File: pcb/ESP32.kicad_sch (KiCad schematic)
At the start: 27 parts, among them J5 SPKR, SW1 BOOT, SW2 RESET, U3 SN74LV1T34DBV, U5 MAX98357A, U8 ESP32-S3-WROOM-2-N32R16V

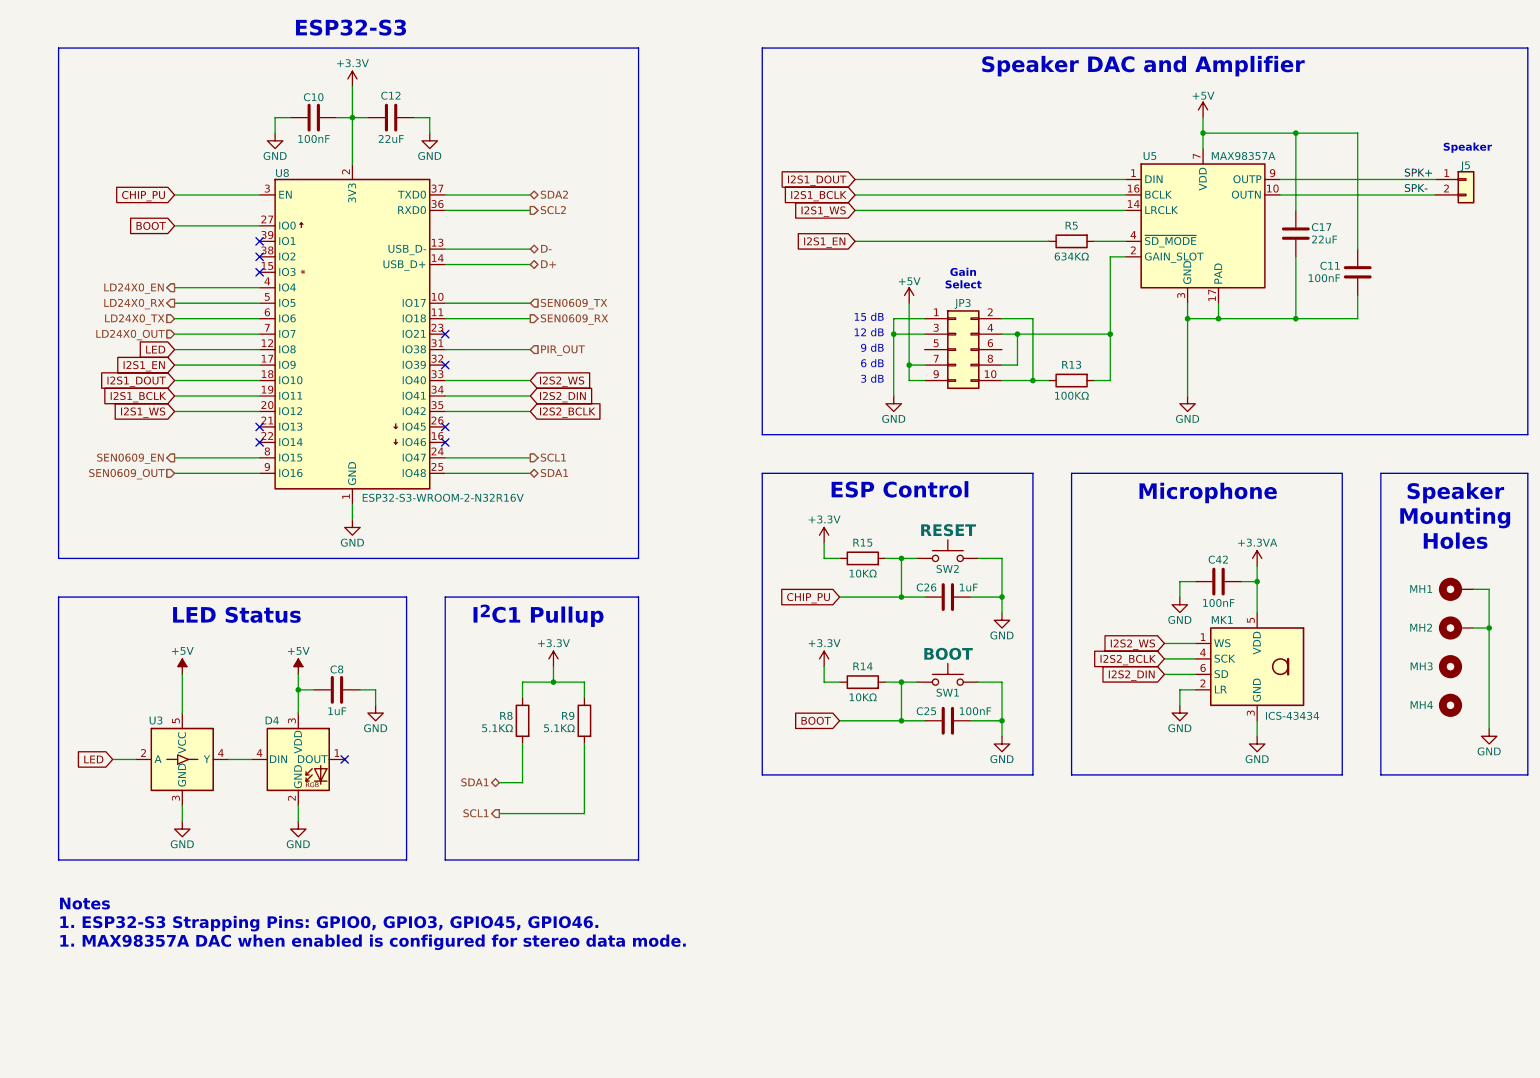
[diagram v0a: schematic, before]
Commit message: Rev A Updates
Support LD2410S and LD2420 Radars in same connector as C4001. Now using 3.3V instead of 5V.
Removed Power control for Radars.
Added DS18S20 to measure CO sensor temperature directly.
Reworked SHT4X layout to reduce thermal transfer.
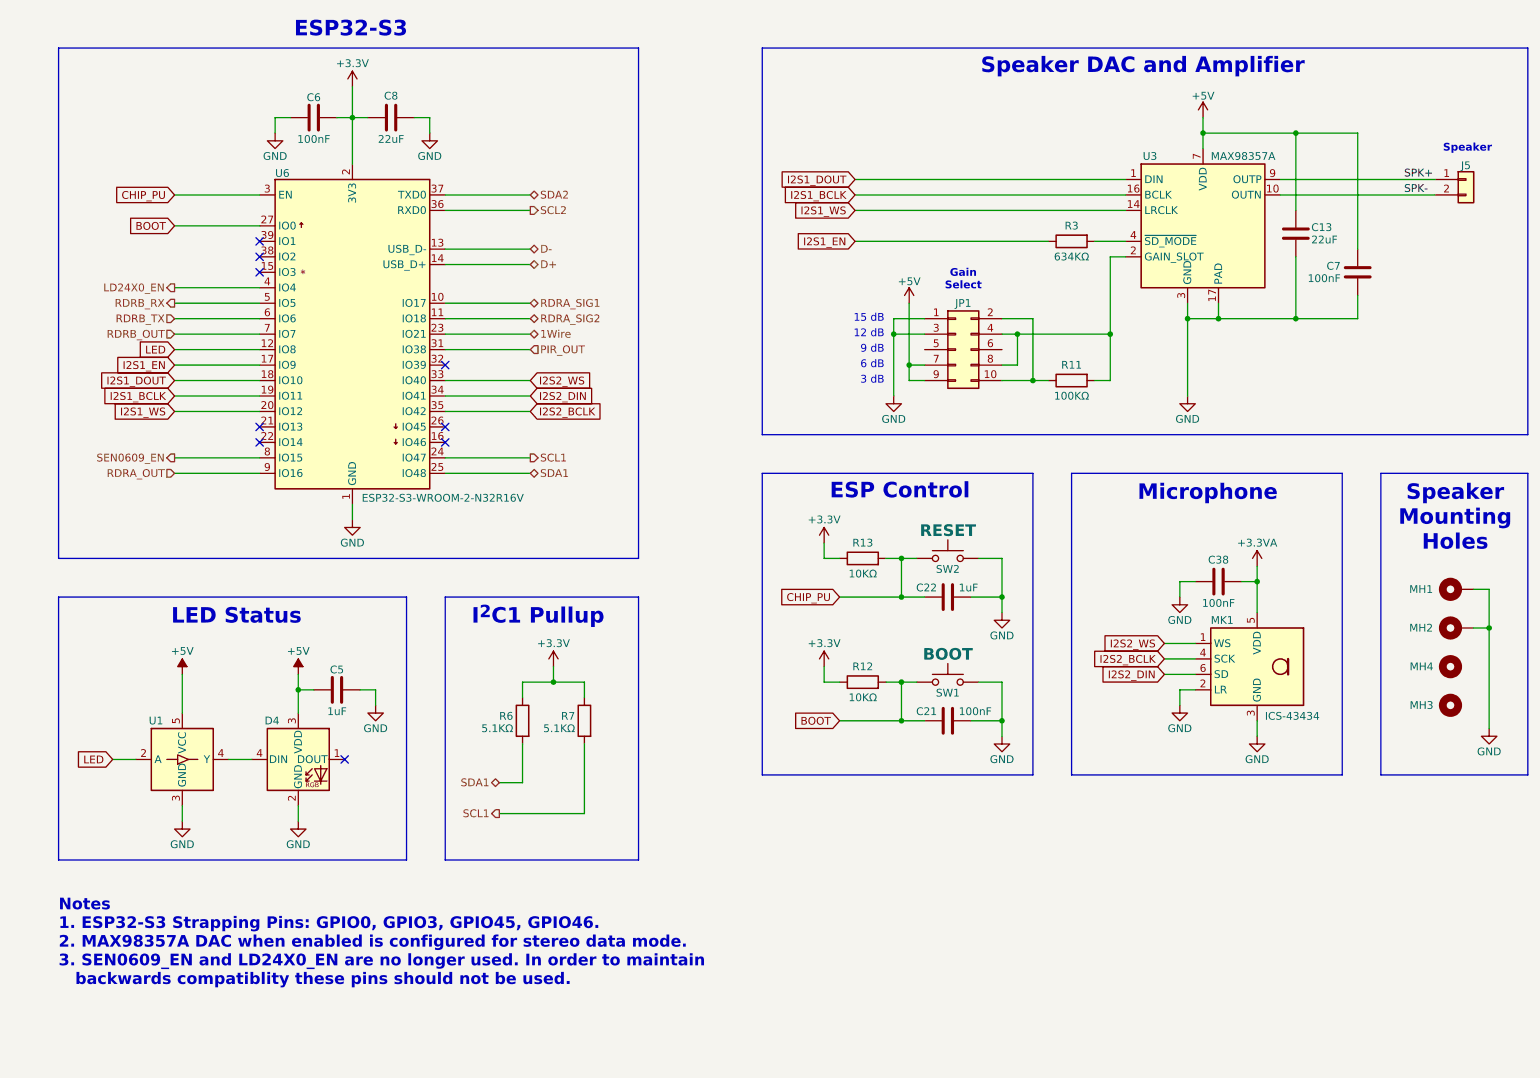
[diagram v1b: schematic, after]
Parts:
- renumbered C17 to C13, C25 to C21, C26 to C22, C42 to C38, C8 to C5, C10 to C6, C11 to C7, C12 to C8, JP3 to JP1, MH4 to MH3, MH3 to MH4, R13 to R11, R14 to R12, R15 to R13, R5 to R3, R8 to R6, R9 to R7, U3 to U1, U5 to U3, U8 to U6
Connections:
- net 1Wire: now reaches U6.23 (IO21)
- net LD24X0_OUT renamed RDRB_OUT
- net LD24X0_RX renamed RDRB_RX
- net LD24X0_TX renamed RDRB_TX
- net SEN0609_OUT renamed RDRA_OUT
- net SEN0609_RX renamed RDRA_SIG2
- net SEN0609_TX renamed RDRA_SIG1
- no-connect marks 10 -> 9
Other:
- note added: "Notes 1. ESP32-S3 Strapping Pins: GPIO0, GPIO3, GPIO45, GPIO46. 2. MAX98357A DAC when enabled is configured for stereo data mode. 3. SEN0609_EN and LD24X0_EN are no longer used. In order to maintain backwards compatiblity these pins should not be used."
- note removed: "Notes 1. ESP32-S3 Strapping Pins: GPIO0, GPIO3, GPIO45, GPIO46. 1. MAX98357A DAC when enabled is configured for stereo data mode."
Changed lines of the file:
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@@
 	(title_block
 		(title "ESPHome Parking Assistant")
-		(date "2025-04-18")
-		(rev "A")
+		(date "2025-09-23")
+		(rev "B")
 		(company "Mike Lawrence")
+		(comment 1 "Rev A: Fixed Rev - mistakes.")
+		(comment 2 "Rev B: Support for LD2410S/LD2420 and temp sensor for CO sensor.")
 	)
 	(rectangle
@@
 		)
 	)
-	(text "Notes\n1. ESP32-S3 Strapping Pins: GPIO0, GPIO3, GPIO45, GPIO46.\n1. MAX98357A DAC when enabled is configured for stereo data mode."
+	(text "Notes\n1. ESP32-S3 Strapping Pins: GPIO0, GPIO3, GPIO45, GPIO46.\n2. MAX98357A DAC when enabled is configured for stereo data mode.\n3. SEN0609_EN and LD24X0_EN are no longer used. In order to maintain\n   backwards compatiblity these pins should not be used."
 		(exclude_from_sim no)
 		(at 25.4 165.1 0)
@@
 	)
 	(no_connect
-		(at 88.9 72.39)
-	)
-	(no_connect
 		(at 58.42 59.69)
 	)
@@
 	(wire
 		(pts
+			(xy 88.9 72.39) (xy 102.87 72.39)
+		)
+		(stroke
+			(width 0)
+			(type default)
+		)
+	)
+	(wire
+		(pts
 			(xy 213.36 39.37) (xy 213.36 41.91)
 		)
@@
 		)
 	)
-	(hierarchical_label "LD24X0_TX"
+	(hierarchical_label "RDRB_TX"
 		(shape input)
 		(at 44.45 69.85 180)
@@
 		)
 	)
-	(hierarchical_label "LD24X0_RX"
+	(hierarchical_label "RDRA_SIG1"
+		(shape bidirectional)
+		(at 102.87 67.31 0)
+		(effects
+			(font
+				(size 1.27 1.27)
+			)
+			(justify left)
+		)
+	)
+	(hierarchical_label "RDRB_RX"
 		(shape output)
 		(at 44.45 67.31 180)
@@
 		)
 	)
-	(hierarchical_label "SEN0609_OUT"
-		(shape input)
-		(at 44.45 95.25 180)
+	(hierarchical_label "1Wire"
+		(shape bidirectional)
+		(at 102.87 72.39 0)
 		(effects
 			(font
 				(size 1.27 1.27)
 			)
-			(justify right)
+			(justify left)
 		)
 	)
-	(hierarchical_label "SEN0609_TX"
+	(hierarchical_label "RDRA_OUT"
 		(shape input)
-		(at 102.87 67.31 0)
+		(at 44.45 95.25 180)
 		(effects
 			(font
 				(size 1.27 1.27)
 			)
-			(justify left)
+			(justify right)
 		)
 	)
@@
 		)
 	)
-	(hierarchical_label "LD24X0_OUT"
+	(hierarchical_label "RDRB_OUT"
 		(shape input)
 		(at 44.45 72.39 180)
@@
 		)
 	)
-	(hierarchical_label "SDA2"
+	(hierarchical_label "RDRA_SIG2"
 		(shape bidirectional)
-		(at 102.87 49.53 0)
+		(at 102.87 69.85 0)
 		(effects
 			(font
@@
 		)
 	)
-	(hierarchical_label "SEN0609_RX"
-		(shape output)
-		(at 102.87 69.85 0)
+	(hierarchical_label "SDA2"
+		(shape bidirectional)
+		(at 102.87 49.53 0)
 		(effects
 			(font
@@
 		(on_board yes)
 		(dnp no)
-		(property "Reference" "MH3"
+		(property "Reference" "MH4"
 			(at 251.206 127 0)
 			(effects
@@
 			(project "ESPHome-Indoor-Multi-Sensor"
 				(path "/e74956a0-c576-42e7-be96-7ce5c3135988/bd75fc22-91af-4c71-b8b1-dfd5c5fbd52d"
-					(reference "MH3")
+					(reference "MH4")
 					(unit 1)
 				)
@@
 		(on_board yes)
 		(dnp no)
-		(property "Reference" "MH4"
+		(property "Reference" "MH3"
 			(at 251.206 133.35 0)
 			(effects
@@
 			(project "ESPHome-Indoor-Multi-Sensor"
 				(path "/e74956a0-c576-42e7-be96-7ce5c3135988/bd75fc22-91af-4c71-b8b1-dfd5c5fbd52d"
-					(reference "MH4")
+					(reference "MH3")
 					(unit 1)
 				)
@@
 		(on_board yes)
 		(dnp no)
-		(property "Reference" "U5"
+		(property "Reference" "U3"
 			(at 203.454 43.18 0)
 			(effects
@@
 			(project "ESPHome-Indoor-Multi-Sensor"
 				(path "/e74956a0-c576-42e7-be96-7ce5c3135988/bd75fc22-91af-4c71-b8b1-dfd5c5fbd52d"
-					(reference "U5")
+					(reference "U3")
 					(unit 1)
 				)
@@
 		(on_board yes)
 		(dnp no)
-		(property "Reference" "R14"
+		(property "Reference" "R12"
 			(at 157.48 127 90)
 			(effects
@@
 			(project "ESPHome-Indoor-Multi-Sensor"
 				(path "/e74956a0-c576-42e7-be96-7ce5c3135988/bd75fc22-91af-4c71-b8b1-dfd5c5fbd52d"
-					(reference "R14")
+					(reference "R12")
 					(unit 1)
 				)
@@
 		(on_board yes)
 		(dnp no)
-		(property "Reference" "C42"
+		(property "Reference" "C38"
 			(at 215.9 109.474 90)
 			(effects
@@
 			(project "ESPHome-Indoor-Multi-Sensor"
 				(path "/e74956a0-c576-42e7-be96-7ce5c3135988/bd75fc22-91af-4c71-b8b1-dfd5c5fbd52d"
-					(reference "C42")
+					(reference "C38")
 					(unit 1)
 				)
@@
 		(on_board yes)
 		(dnp no)
-		(property "Reference" "JP3"
+		(property "Reference" "JP1"
 			(at 173.99 67.31 0)
 			(effects
@@
 			(project "ESPHome-Indoor-Multi-Sensor"
 				(path "/e74956a0-c576-42e7-be96-7ce5c3135988/bd75fc22-91af-4c71-b8b1-dfd5c5fbd52d"
-					(reference "JP3")
+					(reference "JP1")
 					(unit 1)
 				)
@@
 		(on_board yes)
 		(dnp no)
-		(property "Reference" "R13"
+		(property "Reference" "R11"
 			(at 191.77 77.47 90)
 			(effects
@@
 			(project "ESPHome-Indoor-Multi-Sensor"
 				(path "/e74956a0-c576-42e7-be96-7ce5c3135988/bd75fc22-91af-4c71-b8b1-dfd5c5fbd52d"
-					(reference "R13")
+					(reference "R11")
 					(unit 1)
 				)
@@
 		(on_board yes)
 		(dnp no)
-		(property "Reference" "R9"
+		(property "Reference" "R7"
 			(at 110.236 135.128 0)
 			(effects
@@
 			(project "ESPHome-Indoor-Multi-Sensor"
 				(path "/e74956a0-c576-42e7-be96-7ce5c3135988/bd75fc22-91af-4c71-b8b1-dfd5c5fbd52d"
-					(reference "R9")
+					(reference "R7")
 					(unit 1)
 				)
@@
 		(on_board yes)
 		(dnp no)
-		(property "Reference" "U3"
+		(property "Reference" "U1"
 			(at 41.402 135.89 0)
 			(effects
@@
 			(project "ESPHome-Indoor-Multi-Sensor"
 				(path "/e74956a0-c576-42e7-be96-7ce5c3135988/bd75fc22-91af-4c71-b8b1-dfd5c5fbd52d"
-					(reference "U3")
+					(reference "U1")
 					(unit 1)
 				)
@@
 		(on_board yes)
 		(dnp no)
-		(property "Reference" "R8"
+		(property "Reference" "R6"
 			(at 100.076 135.128 0)
 			(effects
@@
 			(project "ESPHome-Indoor-Multi-Sensor"
 				(path "/e74956a0-c576-42e7-be96-7ce5c3135988/bd75fc22-91af-4c71-b8b1-dfd5c5fbd52d"
-					(reference "R8")
+					(reference "R6")
 					(unit 1)
 				)
@@
 		(on_board yes)
 		(dnp no)
-		(property "Reference" "C25"
+		(property "Reference" "C21"
 			(at 169.672 134.366 90)
 			(effects
@@
 			(project "ESPHome-Indoor-Multi-Sensor"
 				(path "/e74956a0-c576-42e7-be96-7ce5c3135988/bd75fc22-91af-4c71-b8b1-dfd5c5fbd52d"
-					(reference "C25")
+					(reference "C21")
 					(unit 1)
 				)
@@
 		(on_board yes)
 		(dnp no)
-		(property "Reference" "R5"
+		(property "Reference" "R3"
 			(at 191.77 54.61 90)
 			(effects
@@
 			(project "ESPHome-Indoor-Multi-Sensor"
 				(path "/e74956a0-c576-42e7-be96-7ce5c3135988/bd75fc22-91af-4c71-b8b1-dfd5c5fbd52d"
-					(reference "R5")
+					(reference "R3")
 					(unit 1)
 				)
@@
 		(on_board yes)
 		(dnp no)
-		(property "Reference" "C12"
+		(property "Reference" "C8"
 			(at 80.01 33.274 90)
 			(effects
@@
 			(project "ESPHome-Indoor-Multi-Sensor"
 				(path "/e74956a0-c576-42e7-be96-7ce5c3135988/bd75fc22-91af-4c71-b8b1-dfd5c5fbd52d"
-					(reference "C12")
+					(reference "C8")
 					(unit 1)
 				)
@@
 		(on_board yes)
 		(dnp no)
-		(property "Reference" "C11"
+		(property "Reference" "C7"
 			(at 235.966 61.214 0)
 			(effects
@@
 			(project "ESPHome-Indoor-Multi-Sensor"
 				(path "/e74956a0-c576-42e7-be96-7ce5c3135988/bd75fc22-91af-4c71-b8b1-dfd5c5fbd52d"
-					(reference "C11")
+					(reference "C7")
 					(unit 1)
 				)
@@
 		(on_board yes)
 		(dnp no)
-		(property "Reference" "R15"
+		(property "Reference" "R13"
 			(at 157.48 106.68 90)
 			(effects
@@
 			(project "ESPHome-Indoor-Multi-Sensor"
 				(path "/e74956a0-c576-42e7-be96-7ce5c3135988/bd75fc22-91af-4c71-b8b1-dfd5c5fbd52d"
-					(reference "R15")
+					(reference "R13")
 					(unit 1)
 				)
@@
 		(on_board yes)
 		(dnp no)
-		(property "Reference" "C10"
+		(property "Reference" "C6"
 			(at 67.31 33.528 90)
 			(effects
@@
 			(project "ESPHome-Indoor-Multi-Sensor"
 				(path "/e74956a0-c576-42e7-be96-7ce5c3135988/bd75fc22-91af-4c71-b8b1-dfd5c5fbd52d"
-					(reference "C10")
+					(reference "C6")
 					(unit 1)
 				)
@@
 		(on_board yes)
 		(dnp no)
-		(property "Reference" "C26"
+		(property "Reference" "C22"
 			(at 169.672 114.046 90)
 			(effects
@@
 			(project "ESPHome-Indoor-Multi-Sensor"
 				(path "/e74956a0-c576-42e7-be96-7ce5c3135988/bd75fc22-91af-4c71-b8b1-dfd5c5fbd52d"
-					(reference "C26")
+					(reference "C22")
 					(unit 1)
 				)
@@
 		(on_board yes)
 		(dnp no)
-		(property "Reference" "U8"
+		(property "Reference" "U6"
 			(at 60.96 45.974 0)
 			(effects
@@
 			(project ""
 				(path "/e74956a0-c576-42e7-be96-7ce5c3135988/bd75fc22-91af-4c71-b8b1-dfd5c5fbd52d"
-					(reference "U8")
+					(reference "U6")
 					(unit 1)
 				)
@@
 		(on_board yes)
 		(dnp no)
-		(property "Reference" "C8"
+		(property "Reference" "C5"
 			(at 71.12 127.508 90)
 			(effects
@@
 			(project "ESPHome-Indoor-Multi-Sensor"
 				(path "/e74956a0-c576-42e7-be96-7ce5c3135988/bd75fc22-91af-4c71-b8b1-dfd5c5fbd52d"
-					(reference "C8")
+					(reference "C5")
 					(unit 1)
 				)
@@
 		(on_board yes)
 		(dnp no)
-		(property "Reference" "C17"
+		(property "Reference" "C13"
 			(at 231.14 54.864 0)
 			(effects
@@
 			(project "ESPHome-Indoor-Multi-Sensor"
 				(path "/e74956a0-c576-42e7-be96-7ce5c3135988/bd75fc22-91af-4c71-b8b1-dfd5c5fbd52d"
-					(reference "C17")
+					(reference "C13")
 					(unit 1)
 				)

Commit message: Cleanup schematic, BOM and update gerber files
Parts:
- removed R6, R7: 5.1KΩ, Resistor_SMD:R_0402_1005Metric, symbol Device:R
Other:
- note removed: "I^{2}C1 Pullup"
- moved on the sheet: C21, C22, C5, R12, R13, SW1, SW2
